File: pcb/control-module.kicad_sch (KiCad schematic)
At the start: 29 parts, among them J1 Screw_Terminal_01x06, J2 Conn_01x07_Pin, SW1 SW_DIP_x04, U1 TPS2116DRL

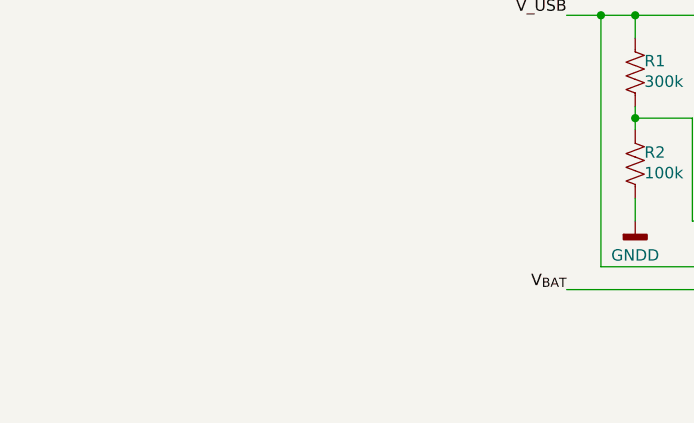
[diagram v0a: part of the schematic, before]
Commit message: Added GPS module in schematic hierarchy
Updated Schematic Hierarchy by adding a new GPS module sheet.
Imported Symbol and footprints for Ublox SAM M10Q GPS module from online source to KiCad Library.
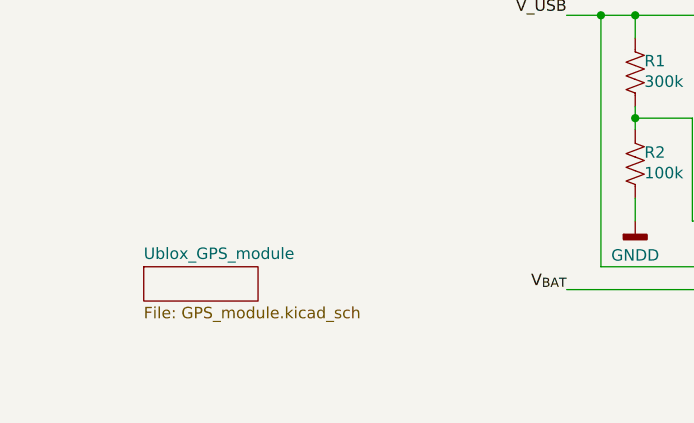
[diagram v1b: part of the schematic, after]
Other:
- added sheet Ublox_GPS_module (GPS_module.kicad_sch)
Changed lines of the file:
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@@
+		)
+	)
+	(sheet
+		(at 29.21 181.61)
+		(size 12.7 3.81)
+		(exclude_from_sim no)
+		(in_bom yes)
+		(on_board yes)
+		(dnp no)
+		(fields_autoplaced yes)
+		(stroke
+			(width 0.1524)
+			(type solid)
+		)
+		(fill
+			(color 0 0 0 0.0000)
+		)
+		(property "Sheetname" "Ublox_GPS_module"
+			(at 29.21 180.8984 0)
+			(effects
+				(font
+					(size 1.27 1.27)
+				)
+				(justify left bottom)
+			)
+		)
+		(property "Sheetfile" "GPS_module.kicad_sch"
+			(at 29.21 186.0046 0)
+			(effects
+				(font
+					(size 1.27 1.27)
+				)
+				(justify left top)
+			)
+		)
+		(instances
+			(project "control-module"
+				(path "/ba7b4294-8d75-4b9e-892f-fb52727887ec"
+					(page "10")
+				)
+			)
 		)
 	)

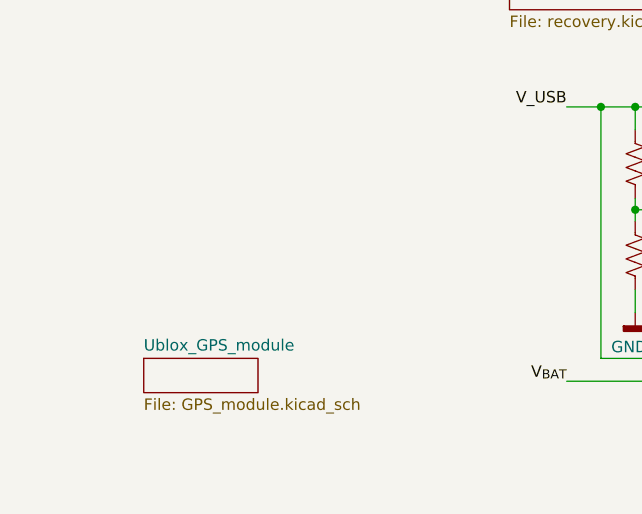
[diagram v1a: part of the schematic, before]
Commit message: Datasheet link attached to footprint
Added datasheet link to footprint and added GND traces.
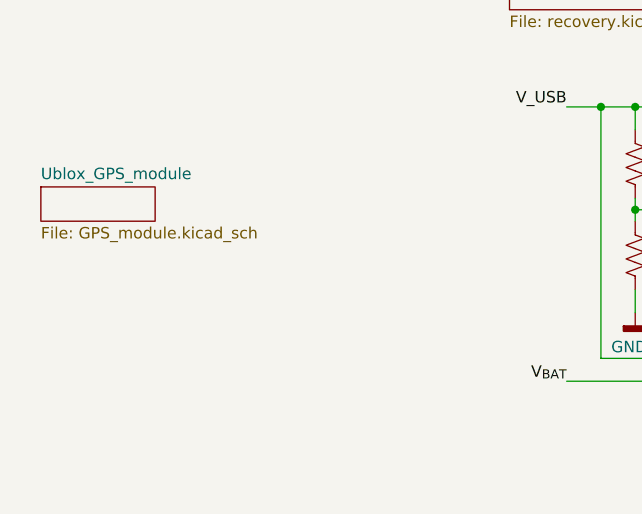
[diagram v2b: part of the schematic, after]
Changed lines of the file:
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@@
 	)
 	(sheet
-		(at 29.21 181.61)
+		(at 17.78 162.56)
 		(size 12.7 3.81)
 		(exclude_from_sim no)
@@
 		)
 		(property "Sheetname" "Ublox_GPS_module"
-			(at 29.21 180.8984 0)
+			(at 17.78 161.8484 0)
 			(effects
 				(font
@@
 		)
 		(property "Sheetfile" "GPS_module.kicad_sch"
-			(at 29.21 186.0046 0)
+			(at 17.78 166.9546 0)
 			(effects
 				(font

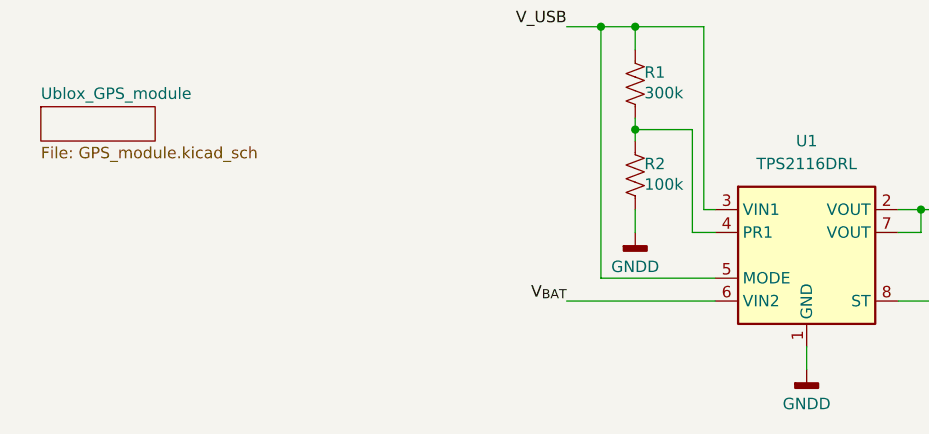
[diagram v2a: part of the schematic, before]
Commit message: transmitter value update
updated some values for transmitter
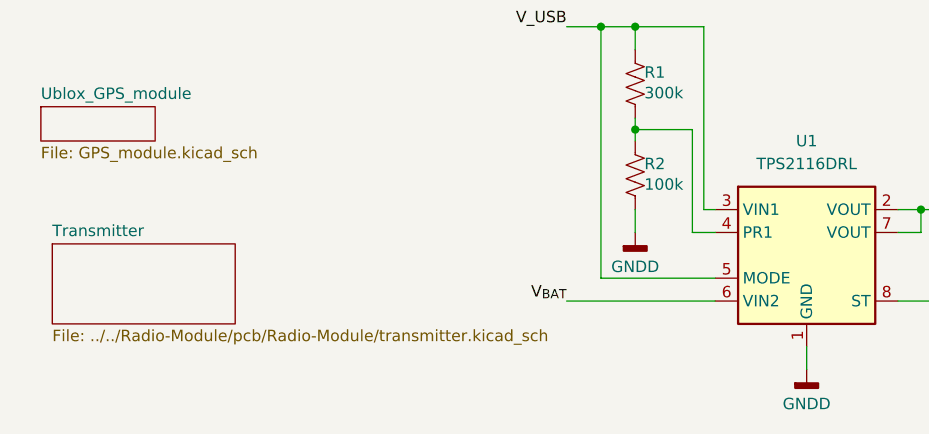
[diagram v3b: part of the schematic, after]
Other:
- added sheet Transmitter (../../Radio-Module/pcb/Radio-Module/transmitter.kicad_sch)
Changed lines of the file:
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@@
+	)
+	(sheet
+		(at 19.05 177.8)
+		(size 20.32 8.89)
+		(exclude_from_sim no)
+		(in_bom yes)
+		(on_board yes)
+		(dnp no)
+		(fields_autoplaced yes)
+		(stroke
+			(width 0.1524)
+			(type solid)
+		)
+		(fill
+			(color 0 0 0 0.0000)
+		)
+		(property "Sheetname" "Transmitter"
+			(at 19.05 177.0884 0)
+			(effects
+				(font
+					(size 1.27 1.27)
+				)
+				(justify left bottom)
+			)
+		)
+		(property "Sheetfile" "../../Radio-Module/pcb/Radio-Module/transmitter.kicad_sch"
+			(at 19.05 187.2746 0)
+			(effects
+				(font
+					(size 1.27 1.27)
+				)
+				(justify left top)
+			)
+		)
+		(instances
+			(project "control-module"
+				(path "/ba7b4294-8d75-4b9e-892f-fb52727887ec"
+					(page "11")
+				)
+			)
+		)
 	)
 	(sheet

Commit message: moved transmitter file
instead of linking transmitter file from local file, moved it into github tracked file
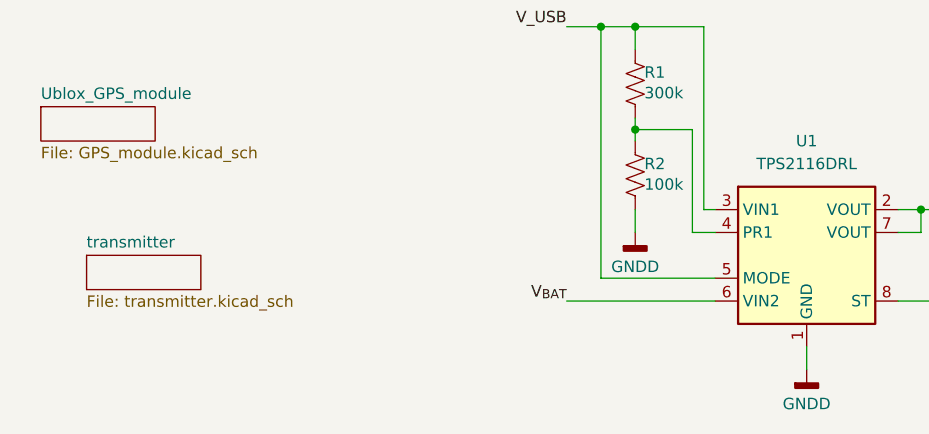
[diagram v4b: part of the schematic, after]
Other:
- removed sheet Transmitter
- added sheet transmitter (transmitter.kicad_sch)
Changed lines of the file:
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@@
 	)
 	(sheet
-		(at 19.05 177.8)
-		(size 20.32 8.89)
+		(at 22.86 179.07)
+		(size 12.7 3.81)
 		(exclude_from_sim no)
 		(in_bom yes)
@@
 			(color 0 0 0 0.0000)
 		)
-		(property "Sheetname" "Transmitter"
-			(at 19.05 177.0884 0)
+		(property "Sheetname" "transmitter"
+			(at 22.86 178.3584 0)
 			(effects
 				(font
@@
 			)
 		)
-		(property "Sheetfile" "../../Radio-Module/pcb/Radio-Module/transmitter.kicad_sch"
-			(at 19.05 187.2746 0)
+		(property "Sheetfile" "transmitter.kicad_sch"
+			(at 22.86 183.4646 0)
 			(effects
 				(font

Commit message: Test Push
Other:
- note added: "Current max board dimensions: 63.5mm x 63.5mm"
- note added: "Notes:"
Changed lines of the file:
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@@
 	)
 	(rectangle
+		(start 20.32 184.15)
+		(end 53.34 201.295)
+		(stroke
+			(width 0)
+			(type default)
+		)
+		(fill
+			(type none)
+		)
+	)
+	(rectangle
 		(start 224.79 132.715)
 		(end 250.19 165.1)
@@
 		)
 	)
+	(text "Notes:"
+		(exclude_from_sim no)
+		(at 23.622 183.134 0)
+		(effects
+			(font
+				(size 1.27 1.27)
+			)
+		)
+	)
 	(text "Divide battery voltage by four to\nfit in ADC range. Will by \nmultiplied by 4 in software."
 		(exclude_from_sim no)
@@
 		)
 	)
+	(text "Current max board dimensions: \n63.5mm x 63.5mm"
+		(exclude_from_sim no)
+		(at 20.828 187.198 0)
+		(effects
+			(font
+				(size 1.27 1.27)
+			)
+			(justify left)
+		)
+	)
 	(text "Only using\n1-bit now"
 		(exclude_from_sim no)
@@
 	)
 	(sheet
-		(at 22.86 179.07)
+		(at 16.51 157.48)
 		(size 12.7 3.81)
 		(exclude_from_sim no)
@@
 		)
 		(property "Sheetname" "transmitter"
-			(at 22.86 178.3584 0)
+			(at 16.51 156.7684 0)
 			(effects
 				(font
@@
 		)
 		(property "Sheetfile" "transmitter.kicad_sch"
-			(at 22.86 183.4646 0)
+			(at 16.51 161.8746 0)
 			(effects
 				(font
@@
 	)
 	(sheet
-		(at 17.78 162.56)
+		(at 16.51 147.32)
 		(size 12.7 3.81)
 		(exclude_from_sim no)
@@
 		)
 		(property "Sheetname" "Ublox_GPS_module"
-			(at 17.78 161.8484 0)
+			(at 16.51 146.6084 0)
 			(effects
 				(font
@@
 		)
 		(property "Sheetfile" "GPS_module.kicad_sch"
-			(at 17.78 166.9546 0)
+			(at 16.51 151.7146 0)
 			(effects
 				(font

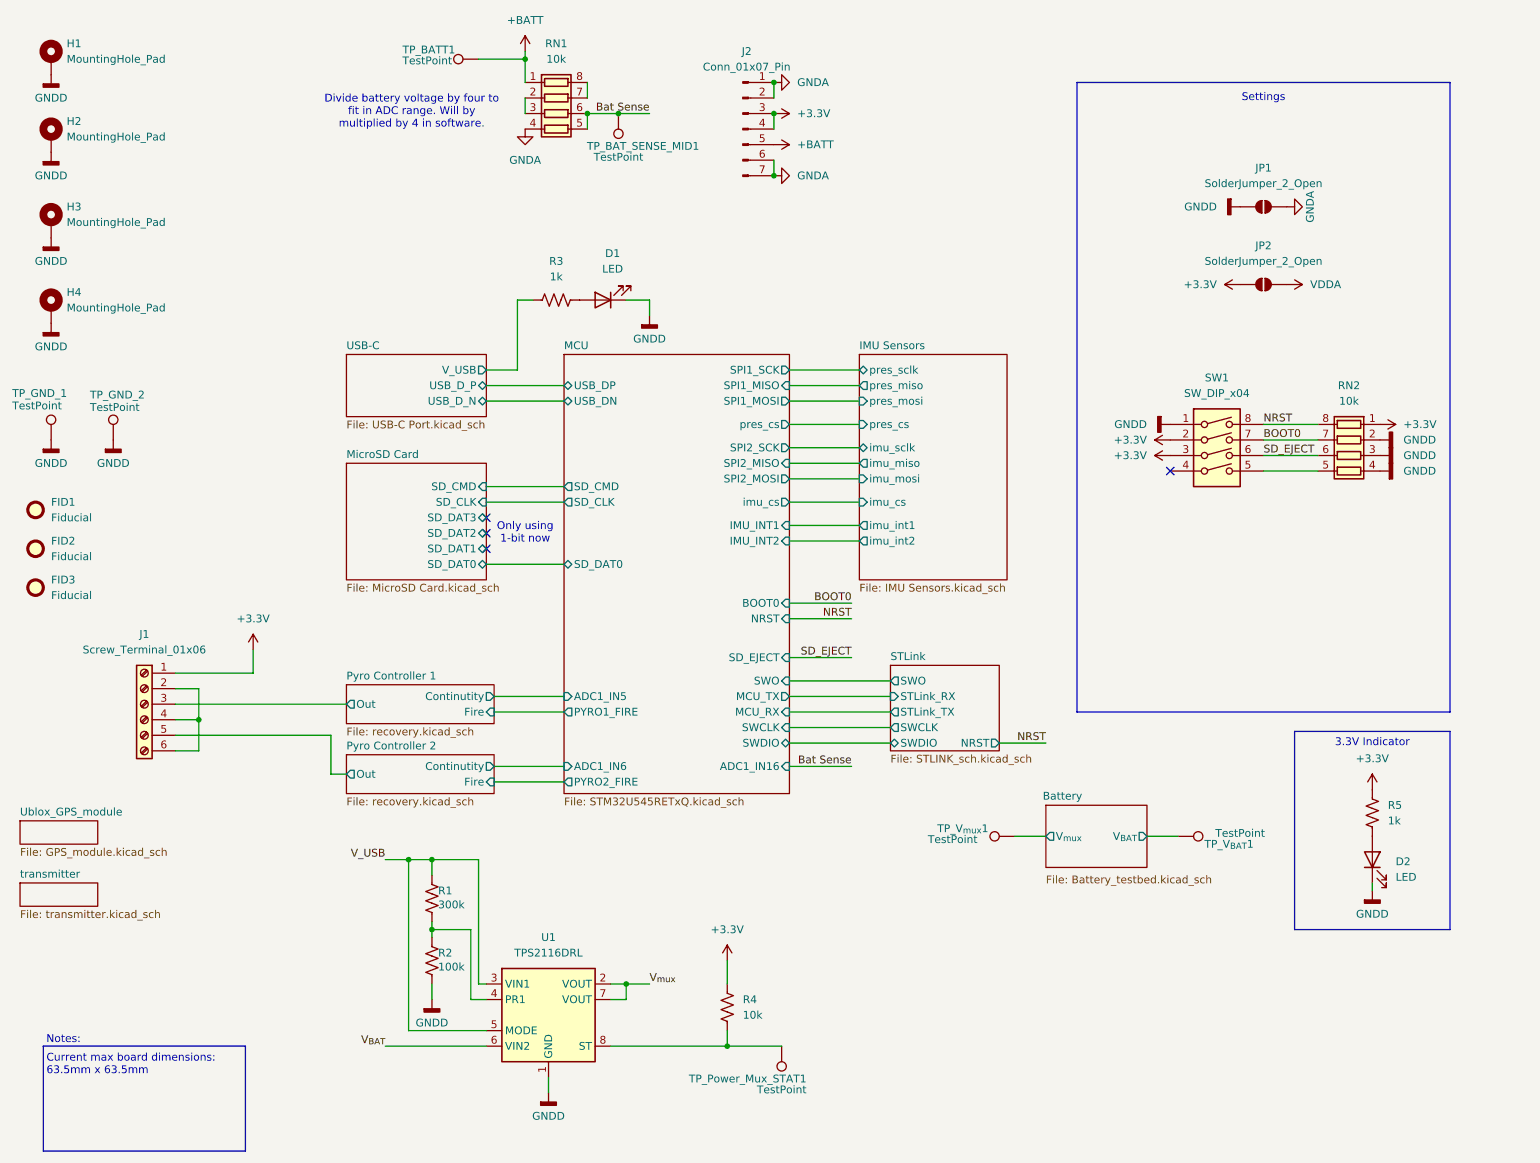
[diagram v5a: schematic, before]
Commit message: Updated schematics and removed most test points
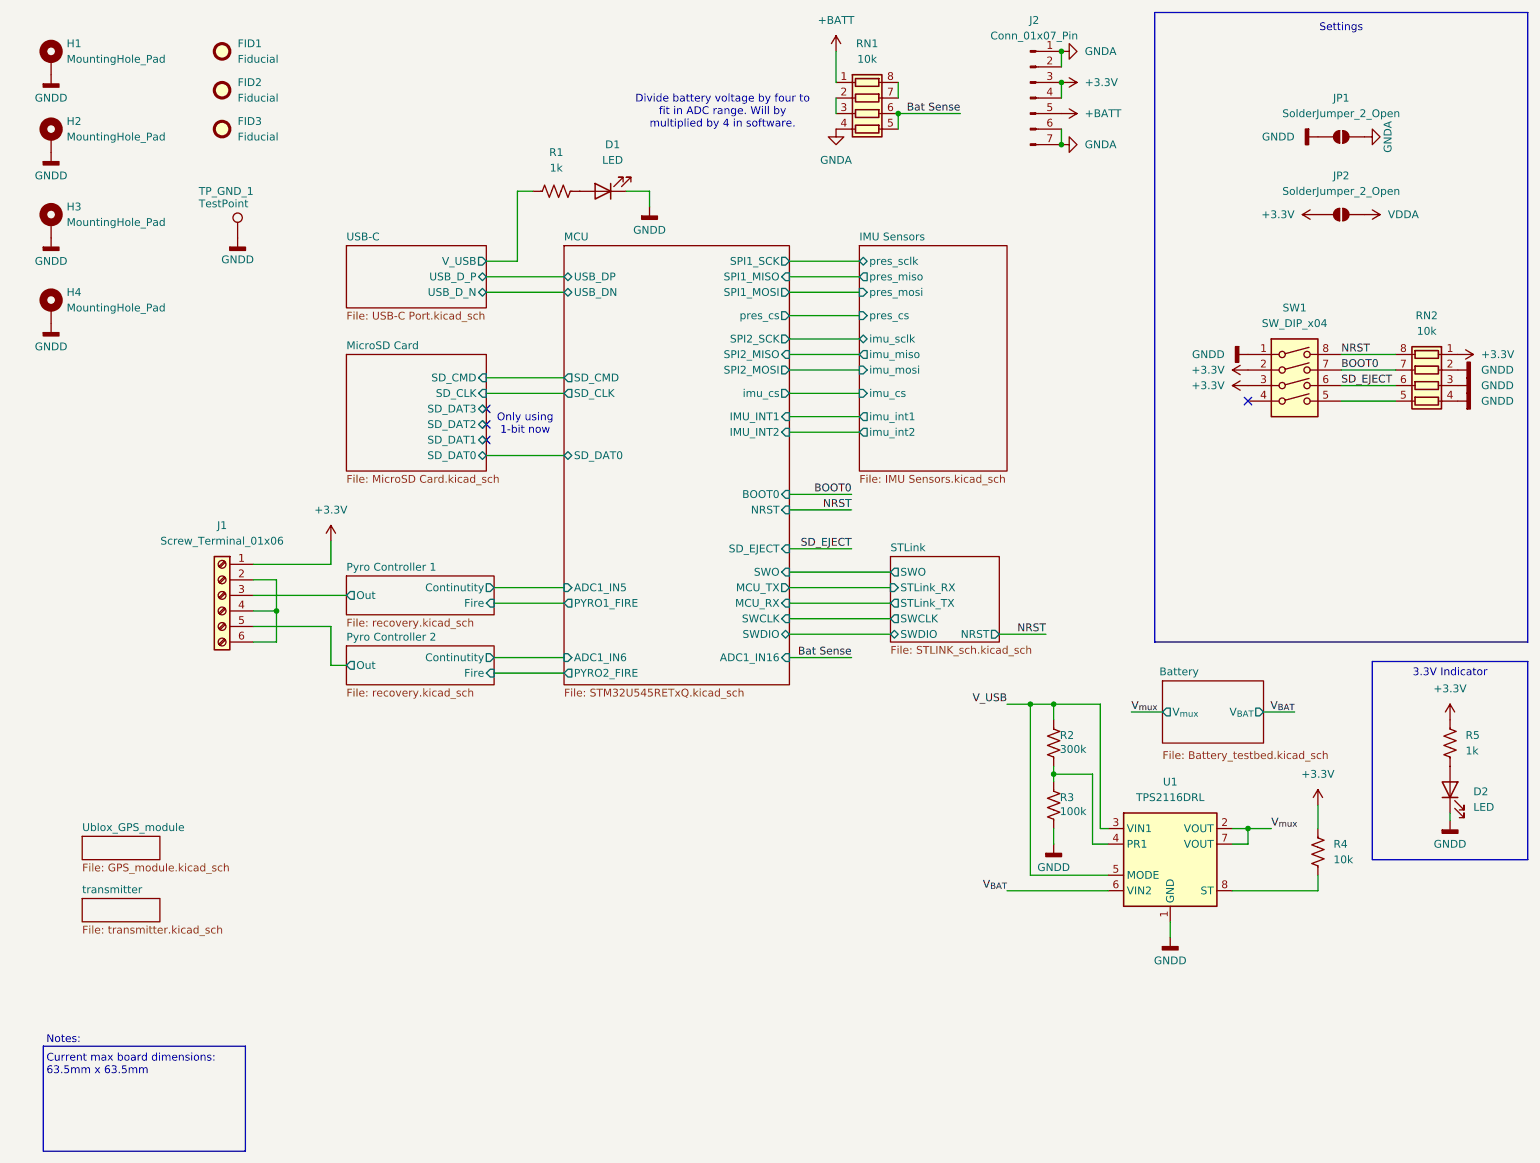
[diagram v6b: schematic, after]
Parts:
- removed TP_BATT1, TP_BAT_SENSE_MID1, TP_GND_2, TP_Power_Mux_STAT1, TP_V_{BAT}1, TP_V_{mux}1: TestPoint, TestPoint:TestPoint_Loop_D2.54mm_Drill1.5mm_Beaded, symbol Connector:TestPoint
- renumbered R3 to R1, R1 to R2, R2 to R3
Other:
- title: Control Module Testbed -> Control Module Rev2
- moved on the sheet: D1, D2, FID1, FID2, FID3, J1, J2, JP1, JP2, R1, R2, R3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

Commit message: Updated Board layout, finalized dimensions
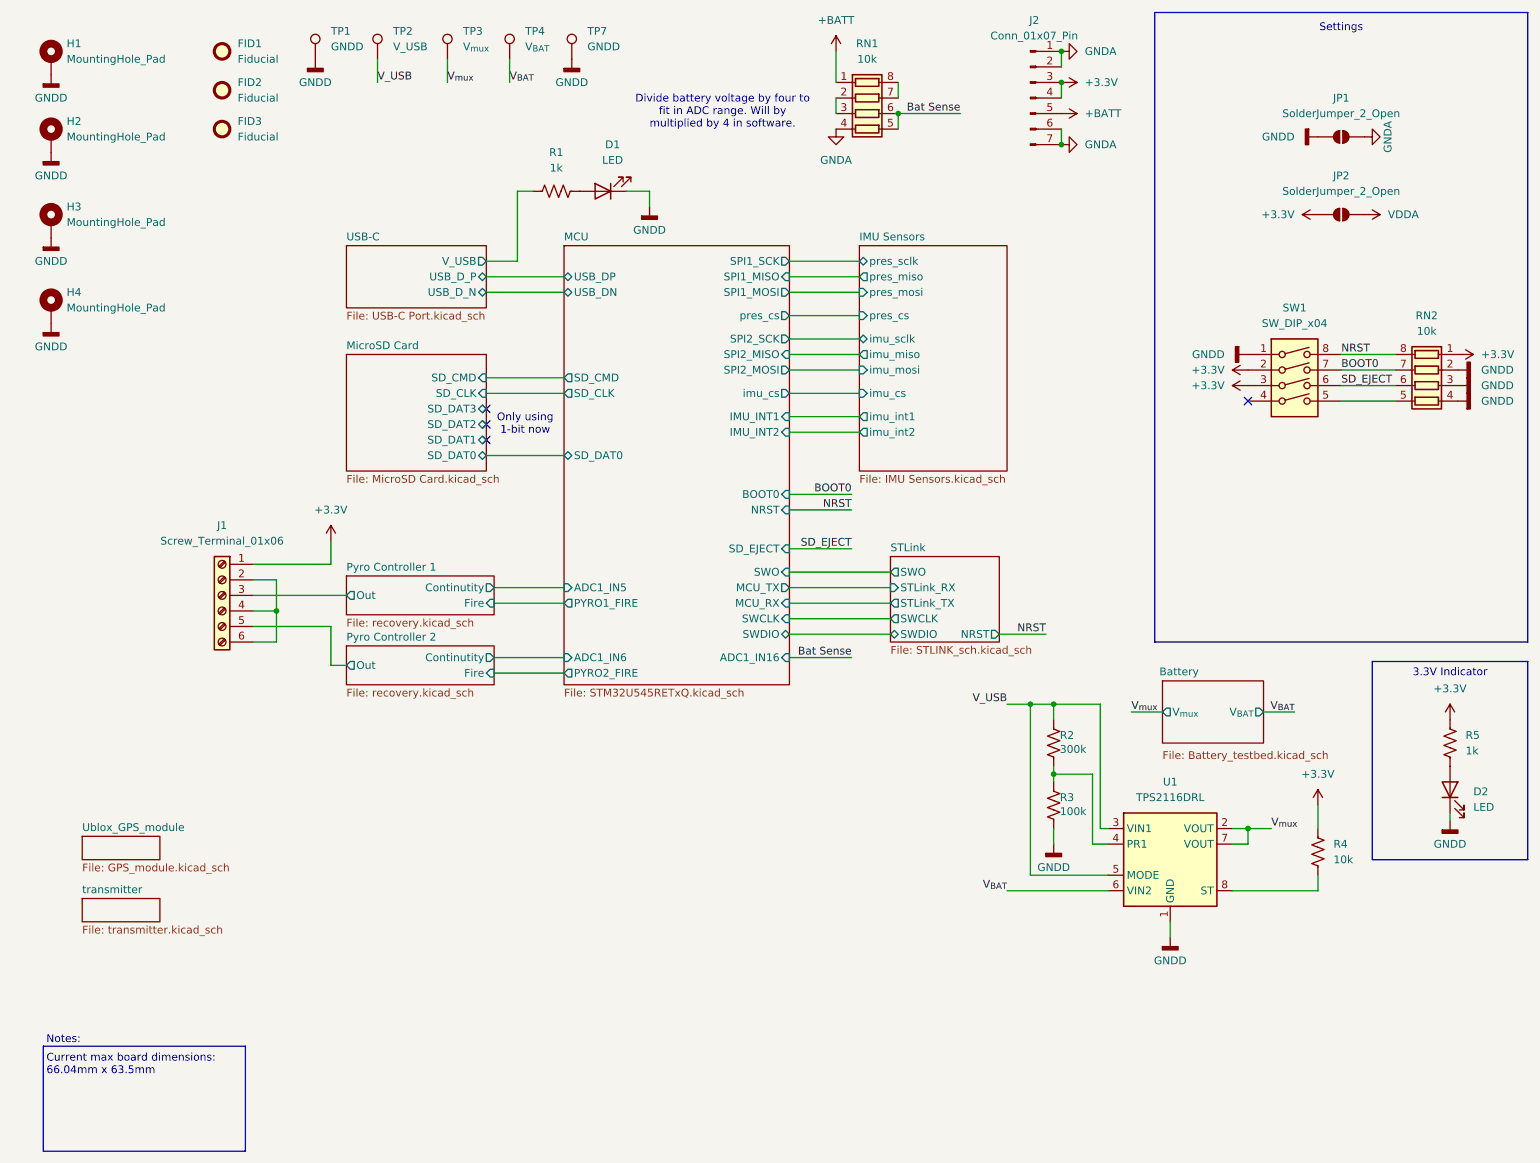
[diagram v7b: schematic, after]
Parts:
- removed TP_GND_1: TestPoint, TestPoint:TestPoint_Loop_D2.54mm_Drill1.5mm_Beaded, symbol Connector:TestPoint
- added TP1, TP7: GNDD, TestPoint:TestPoint_Pad_D1.5mm, symbol Connector:TestPoint
- added TP2: V_USB, TestPoint:TestPoint_Pad_D1.5mm, symbol Connector:TestPoint
- added TP3: V_{mux}, TestPoint:TestPoint_Pad_D1.5mm, symbol Connector:TestPoint
- added TP4: V_{BAT}, TestPoint:TestPoint_Pad_D1.5mm, symbol Connector:TestPoint
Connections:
- net GNDD: now also TP1.1, TP7.1
- net V_USB: now also TP2.1
- net V_{BAT}: now also TP4.1
- net V_{mux}: now also TP3.1
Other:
- note added: "Current max board dimensions: 66.04mm x 63.5mm"
- note removed: "Current max board dimensions: 63.5mm x 63.5mm"
